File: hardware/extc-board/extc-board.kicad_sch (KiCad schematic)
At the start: 18 parts, among them J1 GH link to INT, J2 bus pads, J3 PTSM 0,5/2-HH-SMD 24VAC input, J4 PTSM 0,5/2-HV-SMD 5VDC output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, U1 DS2482-100 (0x18), U3 TMR 12-4811WI

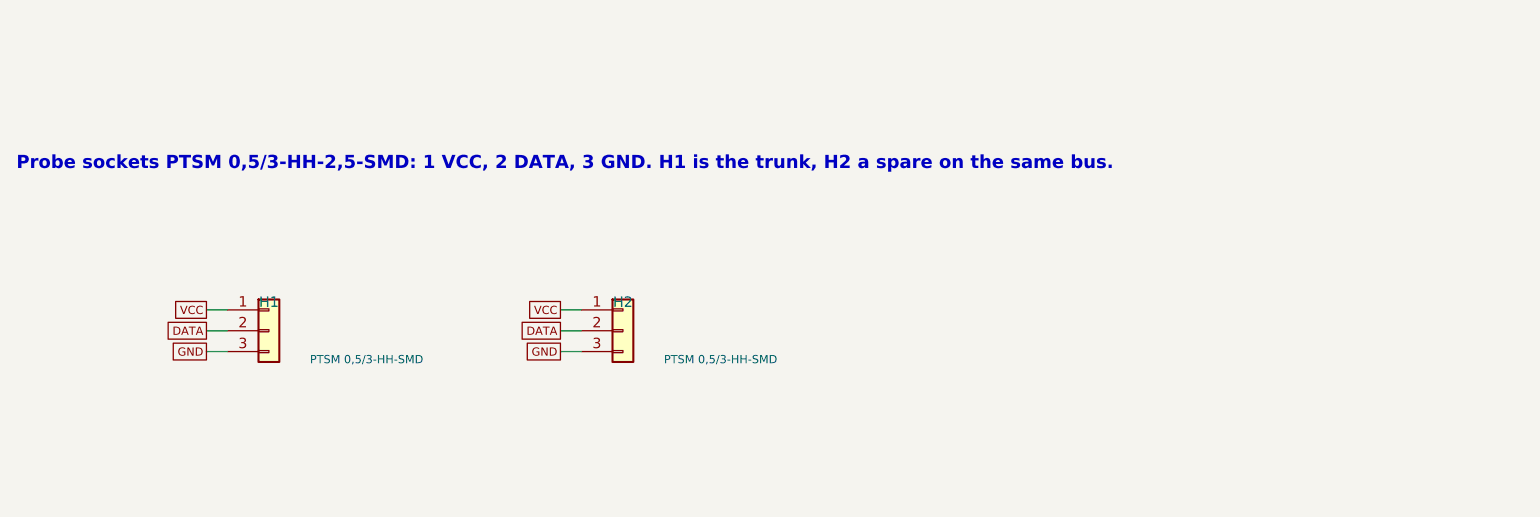
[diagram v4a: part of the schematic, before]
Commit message: Rev C: fit check against the models of the parts being fitted; H1 and H2 are HH0
David supplied the models of the three connectors he is fitting. The
check now lays each on its own footprint: 1808200 on H1 and H2, 1778764
on J3, 1778696 on J4. Every foot lies on its pad and every peg in its
hole.

1808200 is the HH0 header, the HH without its two locating pegs; body,
anchors, leads and latch windows are the same. The footprint keeps its
peg holes, which stay empty under an HH0, so the board takes either.

The board's copper and gerbers are unchanged: only the value of H1 and
H2 in the board, schematic and BOM. DRC is still clean.

The housing check is closed: David confirms a plug seats with the header
faces on the board edge.

Co-Authored-By: Claude Fable 5.1 <noreply@anthropic.com>
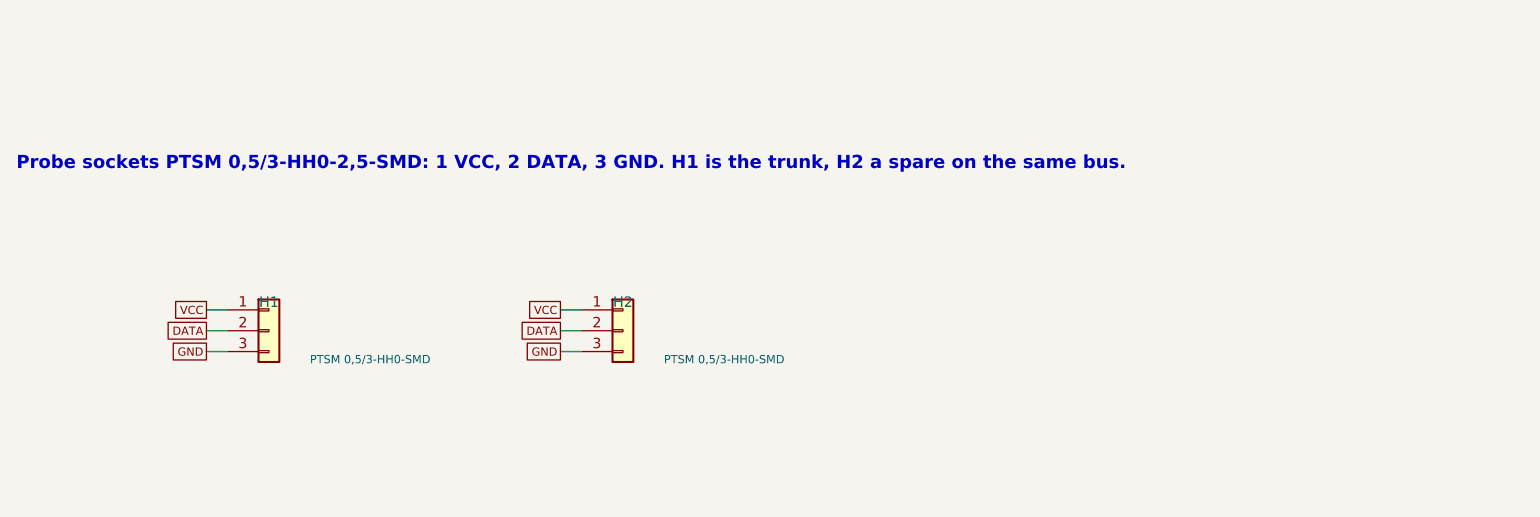
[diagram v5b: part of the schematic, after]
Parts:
- H1, H2: value PTSM 0,5/3-HH-SMD -> PTSM 0,5/3-HH0-SMD
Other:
- note added: "Probe sockets PTSM 0,5/3-HH0-2,5-SMD: 1 VCC, 2 DATA, 3 GND. H1 is the trunk, H2 a spare on the same bus."
- note removed: "Probe sockets PTSM 0,5/3-HH-2,5-SMD: 1 VCC, 2 DATA, 3 GND. H1 is the trunk, H2 a spare on the same bus."
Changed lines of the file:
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@@
 (wire (pts (xy 129.5400 64.7700) (xy 129.5400 67.3100)) (stroke (width 0) (type default)))
 (global_label "GND" (shape passive) (at 129.5400 67.3100 270) (fields_autoplaced yes) (effects (font (size 1.0 1.0)) (justify left)) (property "Intersheetrefs" "${INTERSHEET_REFS}" (at 0 0 0) (effects (font (size 1.27 1.27)) (hide yes))))
-(text "Probe sockets PTSM 0,5/3-HH-2,5-SMD: 1 VCC, 2 DATA, 3 GND. H1 is the trunk, H2 a spare on the same bus." (exclude_from_sim no) (at 20.00 160.00 0) (effects (font (size 1.6 1.6) bold) (justify left)))
-(symbol (lib_id "Connector_Generic:Conn_01x03") (at 50.80 180.34 0) (unit 1) (exclude_from_sim no) (in_bom yes) (on_board yes) (dnp no) (property "Reference" "H1" (at 50.80 176.84 0) (effects (font (size 1.27 1.27)))) (property "Value" "PTSM 0,5/3-HH-SMD" (at 55.80 183.84 0) (effects (font (size 1.0 1.0)) (justify left))) (property "Footprint" "pivac:PTSM_0.5_3-HH-2.5-SMD" (at 50.80 180.34 0) (effects (font (size 1.27 1.27)) (hide yes))) (pin "1") (pin "2") (pin "3") (instances (project "extc-board" (path "/8fcf4daf-789d-447e-a228-91515ee2c90e" (reference "H1") (unit 1)))))
+(text "Probe sockets PTSM 0,5/3-HH0-2,5-SMD: 1 VCC, 2 DATA, 3 GND. H1 is the trunk, H2 a spare on the same bus." (exclude_from_sim no) (at 20.00 160.00 0) (effects (font (size 1.6 1.6) bold) (justify left)))
+(symbol (lib_id "Connector_Generic:Conn_01x03") (at 50.80 180.34 0) (unit 1) (exclude_from_sim no) (in_bom yes) (on_board yes) (dnp no) (property "Reference" "H1" (at 50.80 176.84 0) (effects (font (size 1.27 1.27)))) (property "Value" "PTSM 0,5/3-HH0-SMD" (at 55.80 183.84 0) (effects (font (size 1.0 1.0)) (justify left))) (property "Footprint" "pivac:PTSM_0.5_3-HH-2.5-SMD" (at 50.80 180.34 0) (effects (font (size 1.27 1.27)) (hide yes))) (pin "1") (pin "2") (pin "3") (instances (project "extc-board" (path "/8fcf4daf-789d-447e-a228-91515ee2c90e" (reference "H1") (unit 1)))))
 (wire (pts (xy 45.7200 177.8000) (xy 43.1800 177.8000)) (stroke (width 0) (type default)))
 (global_label "VCC" (shape passive) (at 43.1800 177.8000 180) (fields_autoplaced yes) (effects (font (size 1.0 1.0)) (justify right)) (property "Intersheetrefs" "${INTERSHEET_REFS}" (at 0 0 0) (effects (font (size 1.27 1.27)) (hide yes))))
@@
 (wire (pts (xy 45.7200 182.8800) (xy 43.1800 182.8800)) (stroke (width 0) (type default)))
 (global_label "GND" (shape passive) (at 43.1800 182.8800 180) (fields_autoplaced yes) (effects (font (size 1.0 1.0)) (justify right)) (property "Intersheetrefs" "${INTERSHEET_REFS}" (at 0 0 0) (effects (font (size 1.27 1.27)) (hide yes))))
-(symbol (lib_id "Connector_Generic:Conn_01x03") (at 93.98 180.34 0) (unit 1) (exclude_from_sim no) (in_bom yes) (on_board yes) (dnp no) (property "Reference" "H2" (at 93.98 176.84 0) (effects (font (size 1.27 1.27)))) (property "Value" "PTSM 0,5/3-HH-SMD" (at 98.98 183.84 0) (effects (font (size 1.0 1.0)) (justify left))) (property "Footprint" "pivac:PTSM_0.5_3-HH-2.5-SMD" (at 93.98 180.34 0) (effects (font (size 1.27 1.27)) (hide yes))) (pin "1") (pin "2") (pin "3") (instances (project "extc-board" (path "/8fcf4daf-789d-447e-a228-91515ee2c90e" (reference "H2") (unit 1)))))
+(symbol (lib_id "Connector_Generic:Conn_01x03") (at 93.98 180.34 0) (unit 1) (exclude_from_sim no) (in_bom yes) (on_board yes) (dnp no) (property "Reference" "H2" (at 93.98 176.84 0) (effects (font (size 1.27 1.27)))) (property "Value" "PTSM 0,5/3-HH0-SMD" (at 98.98 183.84 0) (effects (font (size 1.0 1.0)) (justify left))) (property "Footprint" "pivac:PTSM_0.5_3-HH-2.5-SMD" (at 93.98 180.34 0) (effects (font (size 1.27 1.27)) (hide yes))) (pin "1") (pin "2") (pin "3") (instances (project "extc-board" (path "/8fcf4daf-789d-447e-a228-91515ee2c90e" (reference "H2") (unit 1)))))
 (wire (pts (xy 88.9000 177.8000) (xy 86.3600 177.8000)) (stroke (width 0) (type default)))
 (global_label "VCC" (shape passive) (at 86.3600 177.8000 180) (fields_autoplaced yes) (effects (font (size 1.0 1.0)) (justify right)) (property "Intersheetrefs" "${INTERSHEET_REFS}" (at 0 0 0) (effects (font (size 1.27 1.27)) (hide yes))))

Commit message: Rev C: H1 and H2 are 1778777, the 3-way header with locating pegs
David swapped the order from the HH0 header to the HH. Only the part's
value changes in the board, schematic and BOM; copper and gerbers are
as they were.

Co-Authored-By: Claude Fable 5.1 <noreply@anthropic.com>
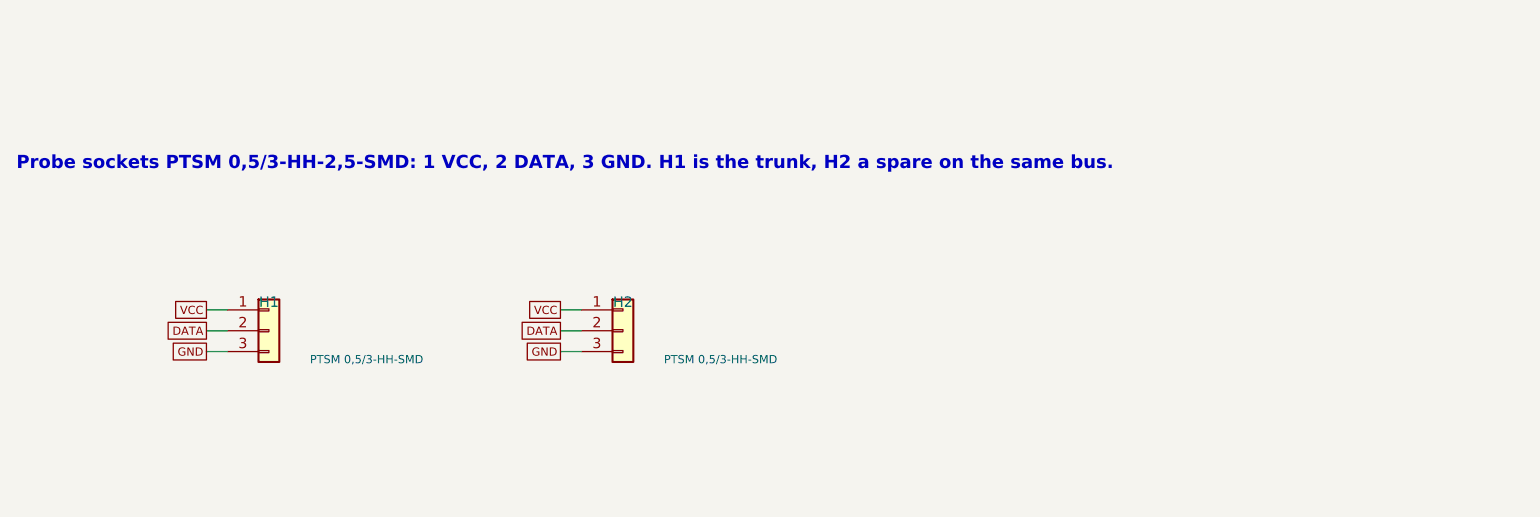
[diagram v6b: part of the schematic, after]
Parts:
- H1, H2: value PTSM 0,5/3-HH0-SMD -> PTSM 0,5/3-HH-SMD
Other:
- note added: "Probe sockets PTSM 0,5/3-HH-2,5-SMD: 1 VCC, 2 DATA, 3 GND. H1 is the trunk, H2 a spare on the same bus."
- note removed: "Probe sockets PTSM 0,5/3-HH0-2,5-SMD: 1 VCC, 2 DATA, 3 GND. H1 is the trunk, H2 a spare on the same bus."
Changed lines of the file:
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@@
 (wire (pts (xy 129.5400 64.7700) (xy 129.5400 67.3100)) (stroke (width 0) (type default)))
 (global_label "GND" (shape passive) (at 129.5400 67.3100 270) (fields_autoplaced yes) (effects (font (size 1.0 1.0)) (justify left)) (property "Intersheetrefs" "${INTERSHEET_REFS}" (at 0 0 0) (effects (font (size 1.27 1.27)) (hide yes))))
-(text "Probe sockets PTSM 0,5/3-HH0-2,5-SMD: 1 VCC, 2 DATA, 3 GND. H1 is the trunk, H2 a spare on the same bus." (exclude_from_sim no) (at 20.00 160.00 0) (effects (font (size 1.6 1.6) bold) (justify left)))
-(symbol (lib_id "Connector_Generic:Conn_01x03") (at 50.80 180.34 0) (unit 1) (exclude_from_sim no) (in_bom yes) (on_board yes) (dnp no) (property "Reference" "H1" (at 50.80 176.84 0) (effects (font (size 1.27 1.27)))) (property "Value" "PTSM 0,5/3-HH0-SMD" (at 55.80 183.84 0) (effects (font (size 1.0 1.0)) (justify left))) (property "Footprint" "pivac:PTSM_0.5_3-HH-2.5-SMD" (at 50.80 180.34 0) (effects (font (size 1.27 1.27)) (hide yes))) (pin "1") (pin "2") (pin "3") (instances (project "extc-board" (path "/8fcf4daf-789d-447e-a228-91515ee2c90e" (reference "H1") (unit 1)))))
+(text "Probe sockets PTSM 0,5/3-HH-2,5-SMD: 1 VCC, 2 DATA, 3 GND. H1 is the trunk, H2 a spare on the same bus." (exclude_from_sim no) (at 20.00 160.00 0) (effects (font (size 1.6 1.6) bold) (justify left)))
+(symbol (lib_id "Connector_Generic:Conn_01x03") (at 50.80 180.34 0) (unit 1) (exclude_from_sim no) (in_bom yes) (on_board yes) (dnp no) (property "Reference" "H1" (at 50.80 176.84 0) (effects (font (size 1.27 1.27)))) (property "Value" "PTSM 0,5/3-HH-SMD" (at 55.80 183.84 0) (effects (font (size 1.0 1.0)) (justify left))) (property "Footprint" "pivac:PTSM_0.5_3-HH-2.5-SMD" (at 50.80 180.34 0) (effects (font (size 1.27 1.27)) (hide yes))) (pin "1") (pin "2") (pin "3") (instances (project "extc-board" (path "/8fcf4daf-789d-447e-a228-91515ee2c90e" (reference "H1") (unit 1)))))
 (wire (pts (xy 45.7200 177.8000) (xy 43.1800 177.8000)) (stroke (width 0) (type default)))
 (global_label "VCC" (shape passive) (at 43.1800 177.8000 180) (fields_autoplaced yes) (effects (font (size 1.0 1.0)) (justify right)) (property "Intersheetrefs" "${INTERSHEET_REFS}" (at 0 0 0) (effects (font (size 1.27 1.27)) (hide yes))))
@@
 (wire (pts (xy 45.7200 182.8800) (xy 43.1800 182.8800)) (stroke (width 0) (type default)))
 (global_label "GND" (shape passive) (at 43.1800 182.8800 180) (fields_autoplaced yes) (effects (font (size 1.0 1.0)) (justify right)) (property "Intersheetrefs" "${INTERSHEET_REFS}" (at 0 0 0) (effects (font (size 1.27 1.27)) (hide yes))))
-(symbol (lib_id "Connector_Generic:Conn_01x03") (at 93.98 180.34 0) (unit 1) (exclude_from_sim no) (in_bom yes) (on_board yes) (dnp no) (property "Reference" "H2" (at 93.98 176.84 0) (effects (font (size 1.27 1.27)))) (property "Value" "PTSM 0,5/3-HH0-SMD" (at 98.98 183.84 0) (effects (font (size 1.0 1.0)) (justify left))) (property "Footprint" "pivac:PTSM_0.5_3-HH-2.5-SMD" (at 93.98 180.34 0) (effects (font (size 1.27 1.27)) (hide yes))) (pin "1") (pin "2") (pin "3") (instances (project "extc-board" (path "/8fcf4daf-789d-447e-a228-91515ee2c90e" (reference "H2") (unit 1)))))
+(symbol (lib_id "Connector_Generic:Conn_01x03") (at 93.98 180.34 0) (unit 1) (exclude_from_sim no) (in_bom yes) (on_board yes) (dnp no) (property "Reference" "H2" (at 93.98 176.84 0) (effects (font (size 1.27 1.27)))) (property "Value" "PTSM 0,5/3-HH-SMD" (at 98.98 183.84 0) (effects (font (size 1.0 1.0)) (justify left))) (property "Footprint" "pivac:PTSM_0.5_3-HH-2.5-SMD" (at 93.98 180.34 0) (effects (font (size 1.27 1.27)) (hide yes))) (pin "1") (pin "2") (pin "3") (instances (project "extc-board" (path "/8fcf4daf-789d-447e-a228-91515ee2c90e" (reference "H2") (unit 1)))))
 (wire (pts (xy 88.9000 177.8000) (xy 86.3600 177.8000)) (stroke (width 0) (type default)))
 (global_label "VCC" (shape passive) (at 86.3600 177.8000 180) (fields_autoplaced yes) (effects (font (size 1.0 1.0)) (justify right)) (property "Intersheetrefs" "${INTERSHEET_REFS}" (at 0 0 0) (effects (font (size 1.27 1.27)) (hide yes))))
